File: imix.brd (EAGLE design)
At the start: 87 x 102.5 mm, 161 parts, among them Q1 AO3418, Q2 AO3415, Q3 AO3415, Q4 AO3415, Q5 AO3415, U1 BQ2423X, U10 ISL29035, U11 FX0S8700CQ, U12 296-12686-1-ND, U3 TLV3202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

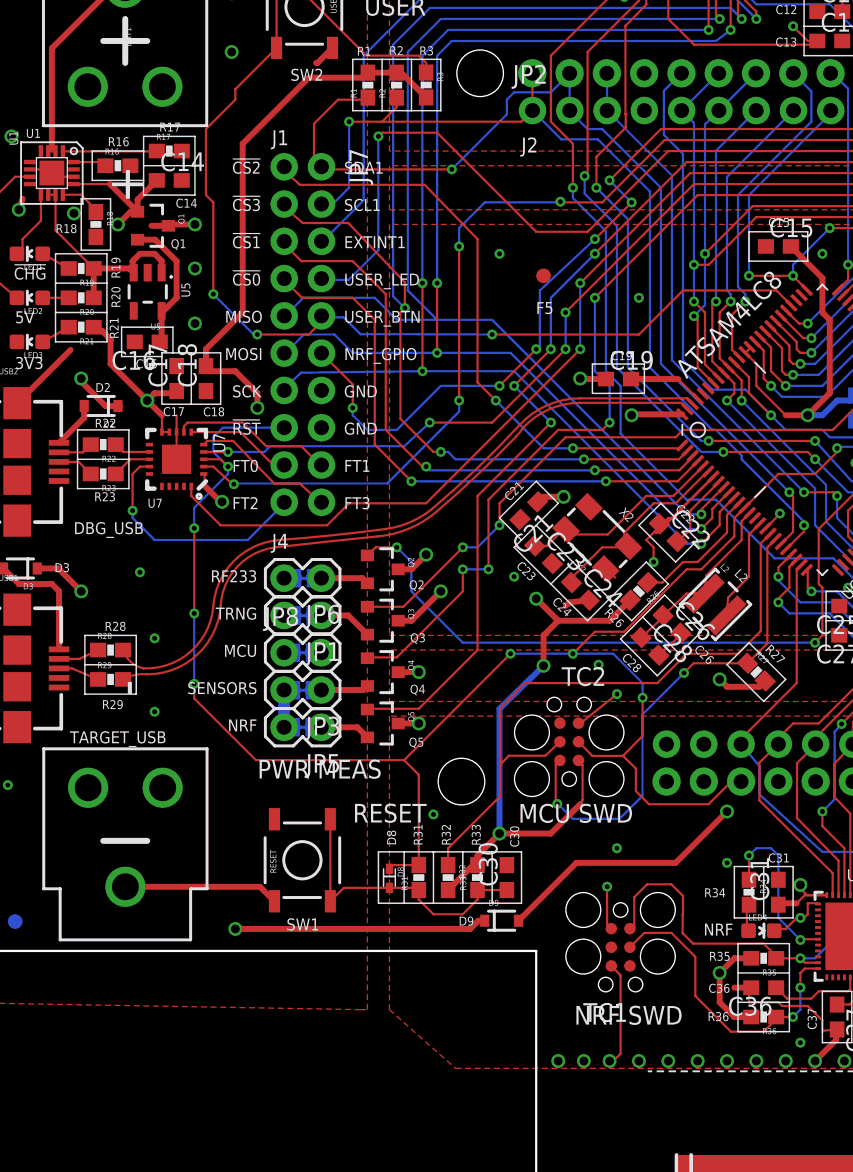
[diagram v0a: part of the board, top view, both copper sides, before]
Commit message: Move MCU SWD to be accessible when a shield is present
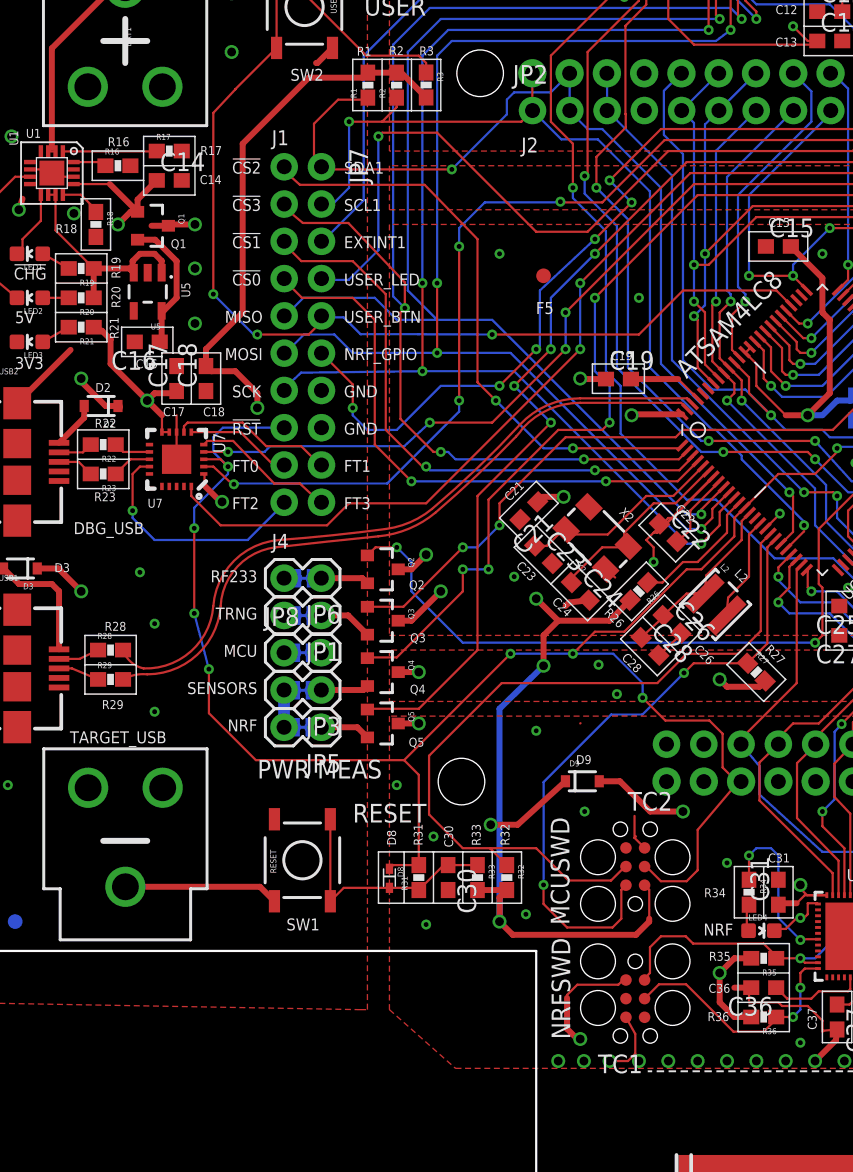
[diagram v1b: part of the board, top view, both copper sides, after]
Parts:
- moved D9 11.0 mm to (40.6, 11.6)
- moved TC2 9.62 mm to (44.2, 5.75)
- moved C30 4.00 mm to (31.5, 5.00), turned to 270 degrees
- moved R32 4.00 mm to (35.5, 5.00)
- moved TC1 3.64 mm to (44.2, -3.25)
- turned R33 to 270 degrees
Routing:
- net VCC_IN: track 96.0 -> 83.6 mm
- net SWDCLK/TCK: track 43.7 -> 54.3 mm
- net SWDIO/TMS: track 33.4 -> 43.4 mm
- net VCC_MCU_3V3: track 165.6 -> 174.6 mm
- net VCC_EXT_5V: track 78.4 -> 70.7 mm
- net NRF_SWDIO: track 77.5 -> 73.4 mm
- net NRF_SWDCLK: track 21.1 -> 17.1 mm
- net VCC_SENSE_3V3: track 91.4 -> 87.6 mm
- net N$8: track 20.2 -> 16.8 mm
- net GND: track 166.1 -> 162.7 mm, vias 80 -> 84
- net VCC_NRF_3V3: track 51.8 -> 54.9 mm
- net !RESET: track 140.6 -> 143.4 mm
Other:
- board text added: "MCUSWD"
- board text added: "NRFSWD"
- board text removed: "MCU SWD"
- board text removed: "NRF SWD"

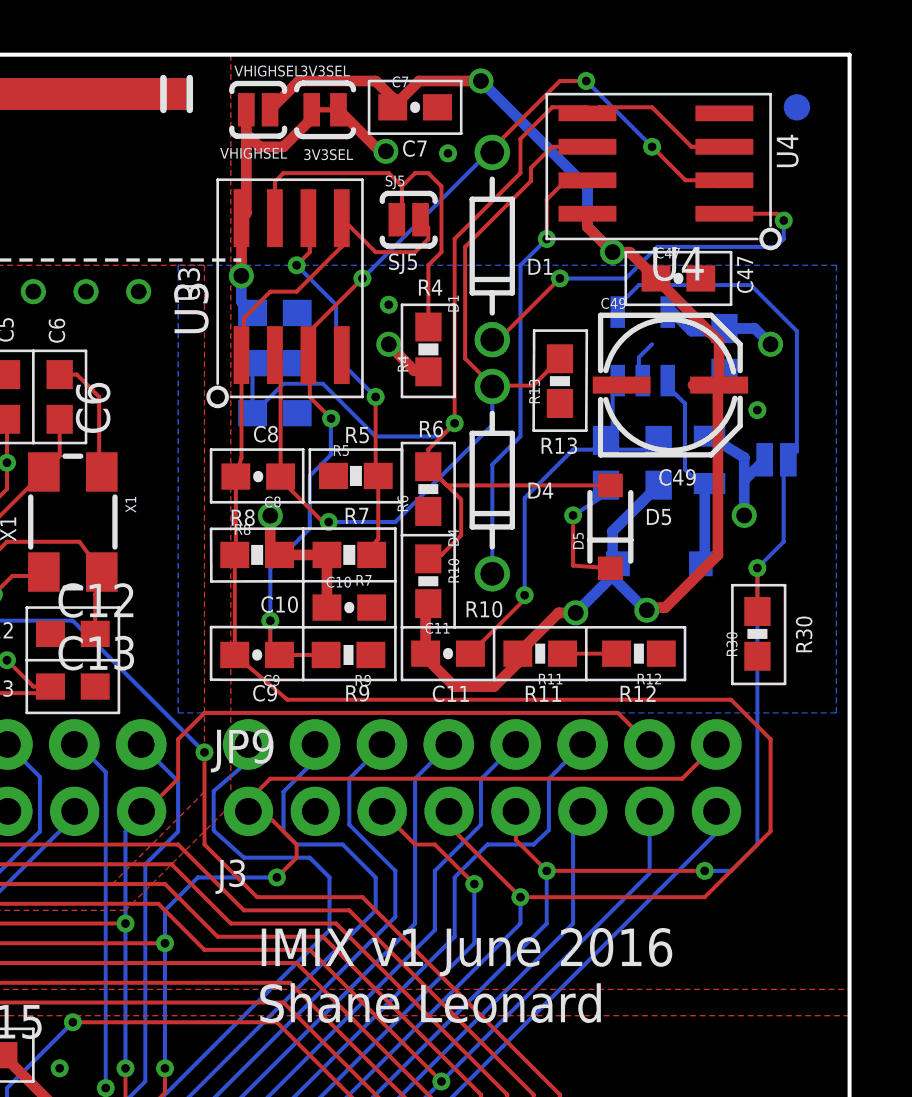
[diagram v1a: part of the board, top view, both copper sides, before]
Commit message: Refactor RNG
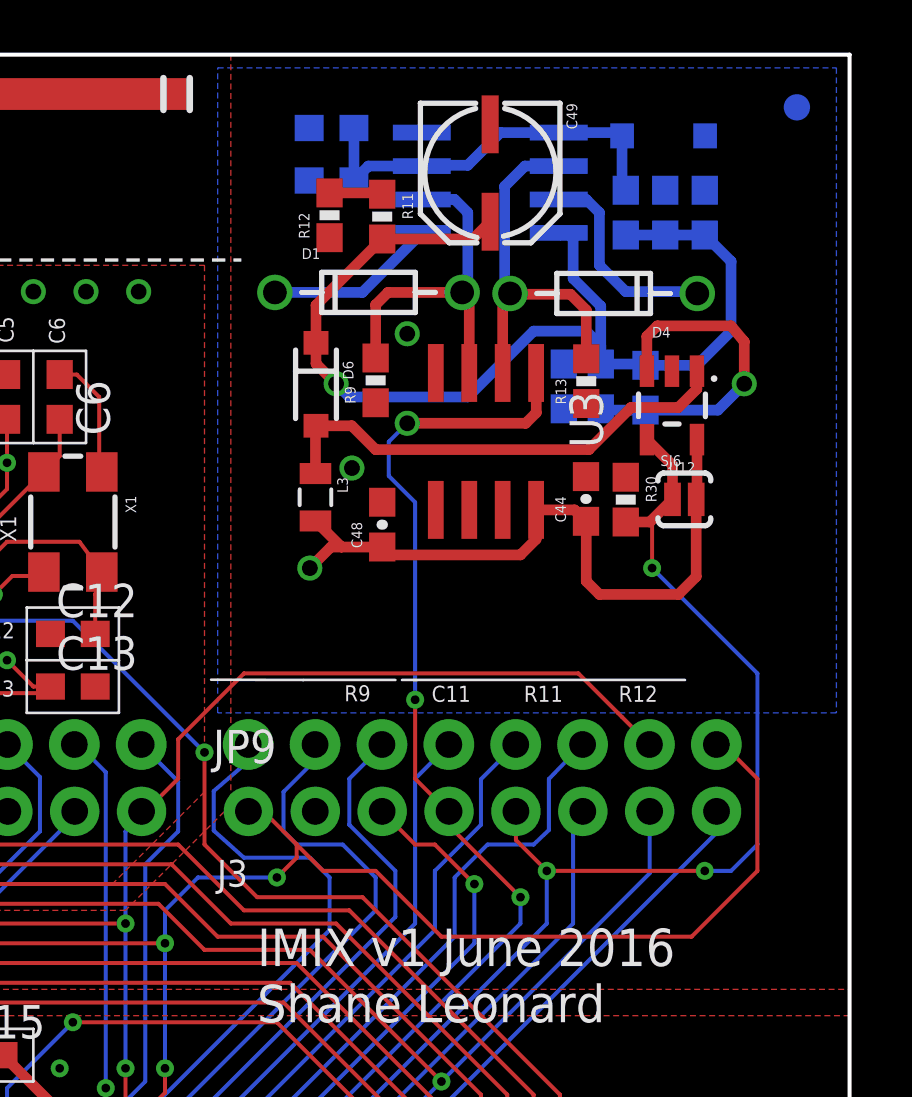
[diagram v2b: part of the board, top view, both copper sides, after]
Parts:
- removed 3V3SEL: SOLDERJUMPER-OLDTRACE, SparkFun-Retired:SJ_2S-TRACE
- removed C10, C8, C9: DNP, SparkFun-Capacitors:0603-CAP
- removed R4, R5, R7, R8: DNP, SparkFun-Passives:0603-RES
- removed R6: DNP, SparkFun-Resistors:0603-RES
- removed SJ5: SOLDERJUMPERNO, SparkFun-Retired:SJ_2S-NO
- removed VHIGHSEL: SOLDERJUMPER-OLDNO, SparkFun-Retired:SJ_2S-NO
- moved R12 20.4 mm to (67.2, 79.9), turned to 90 degrees
- moved R11 17.7 mm to (69.2, 79.8), turned to 270 degrees
- moved R10 15.9 mm to (78.5, 80.0), flipped to the bottom
- moved L3 15.0 mm to (66.7, 69.2), flipped to the top, turned to 270 degrees
- moved D5 15.0 mm to (79.9, 82.9), flipped to the bottom, turned to 0 degrees
- moved D6 14.7 mm to (66.7, 73.5), flipped to the top, turned to 270 degrees
- moved C48 14.6 mm to (69.2, 68.2), flipped to the top, turned to 90 degrees
- moved C44 13.8 mm to (77.0, 69.1), flipped to the top, turned to 90 degrees
- moved C11 12.6 mm to (79.2, 73.3), flipped to the bottom, turned to 270 degrees
- moved R9 10.5 mm to (69.0, 73.6), turned to 90 degrees
- moved C7 10.3 mm to (80.0, 80.0), flipped to the bottom, turned to 90 degrees
- moved C49 10.3 mm to (73.5, 81.6), turned to 270 degrees
- moved U3 9.44 mm to (73.2, 71.3), turned to 180 degrees
- moved C45 9.19 mm to (67.3, 83.2), turned to 0 degrees
- moved C46 9.10 mm to (67.3, 81.2), turned to 0 degrees
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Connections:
- removed net BUFFER: R4.2, SJ5.1, U3.7
- removed net N$67: R5.2, R7.1, U3.6
- removed net N$68: 3V3SEL.1, C44.1, U3.8, VHIGHSEL.1
- net GND: no longer C10.2, R5.1, R6.1
- net N$66: no longer R6.2
- net NOISE1: no longer C9.1
- net NOISE2: no longer C8.1
- net TRNG_OUT: no longer C8.2, C9.2, R8.1, SJ5.2, U3.5
- net VCC_TRNG_3V3: now also C44.1, U3.8; no longer 3V3SEL.2, C10.1, R4.1, R7.2, R8.2
- net VHIGH: no longer VHIGHSEL.2
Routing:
- net TRNG_OUT: track 83.1 -> 45.4 mm, vias 2 -> 4
- net N$66: track 46.3 -> 15.1 mm, vias 1 -> 0
- net NOISE1: track 37.1 -> 13.7 mm, vias 5 -> 0
- net NOISE2: track 32.3 -> 14.7 mm, vias 1 -> 0
- net BUFFER: track 15.4 -> 0.00 mm
- net VHIGH: track 57.3 -> 42.0 mm, vias 4 -> 1
- net N$67: track 14.4 -> 0.00 mm, vias 2 -> 0
- net TRNG_EN: track 62.5 -> 50.2 mm
- net N$68: track 11.4 -> 0.00 mm, vias 1 -> 0
- net N$43: track 8.52 -> 18.3 mm
- net N$51: track 15.7 -> 6.52 mm, vias 2 -> 0
- net N$52: track 17.0 -> 7.91 mm, vias 1 -> 0
- net GND: track 162.7 -> 155.2 mm, vias 84 -> 82
- net VCC_TRNG_3V3: track 96.6 -> 103.5 mm, vias 6 -> 2
- net USART3_RX: track 93.0 -> 99.5 mm
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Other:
- board text removed: "3V3SEL"
- board text removed: "C10"
- board text removed: "C8"
- board text removed: "C9"
- board text removed: "F2"
- board text removed: "R4"
- board text removed: "R5"
- board text removed: "R6"
- board text removed: "R7"
- board text removed: "R8"
- board text removed: "SJ5"
- board text removed: "SJ6"
- board text removed: "VHIGHSEL"

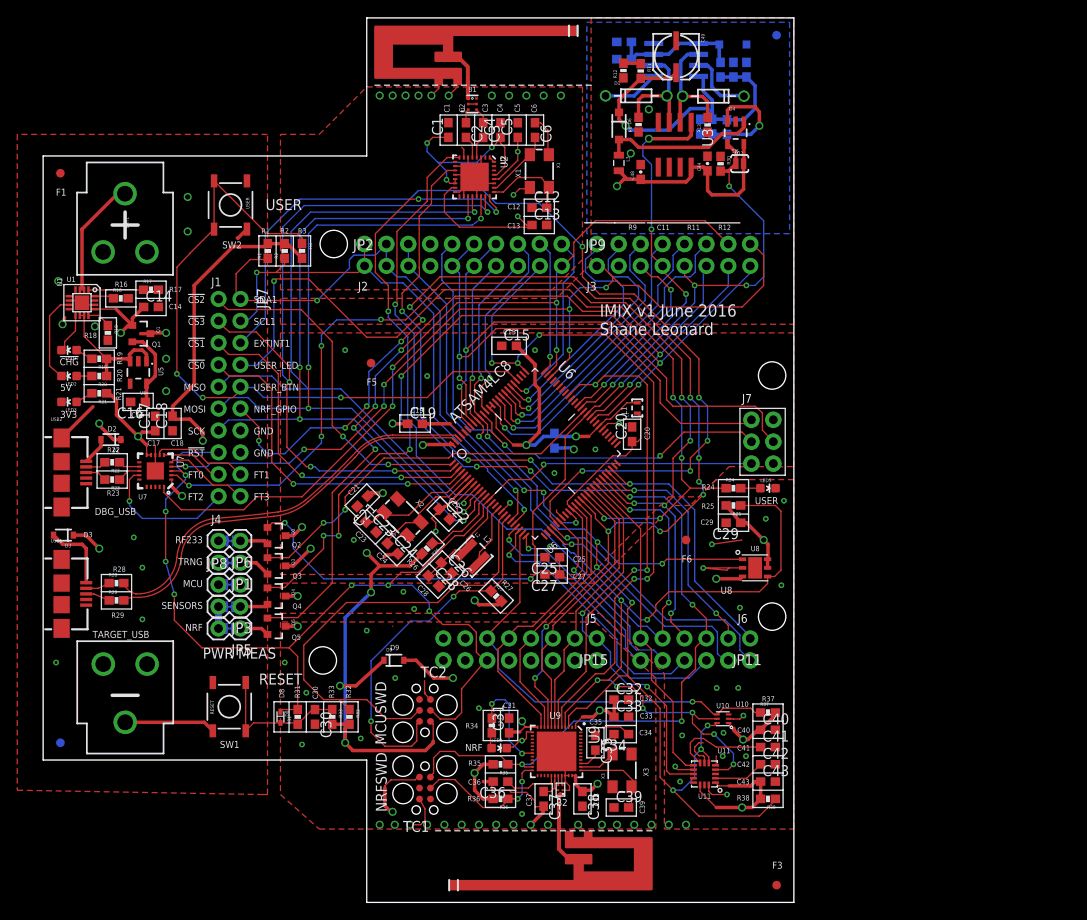
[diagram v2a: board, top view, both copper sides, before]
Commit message: Updated version incorporating several suggestions, still rerouting RNG
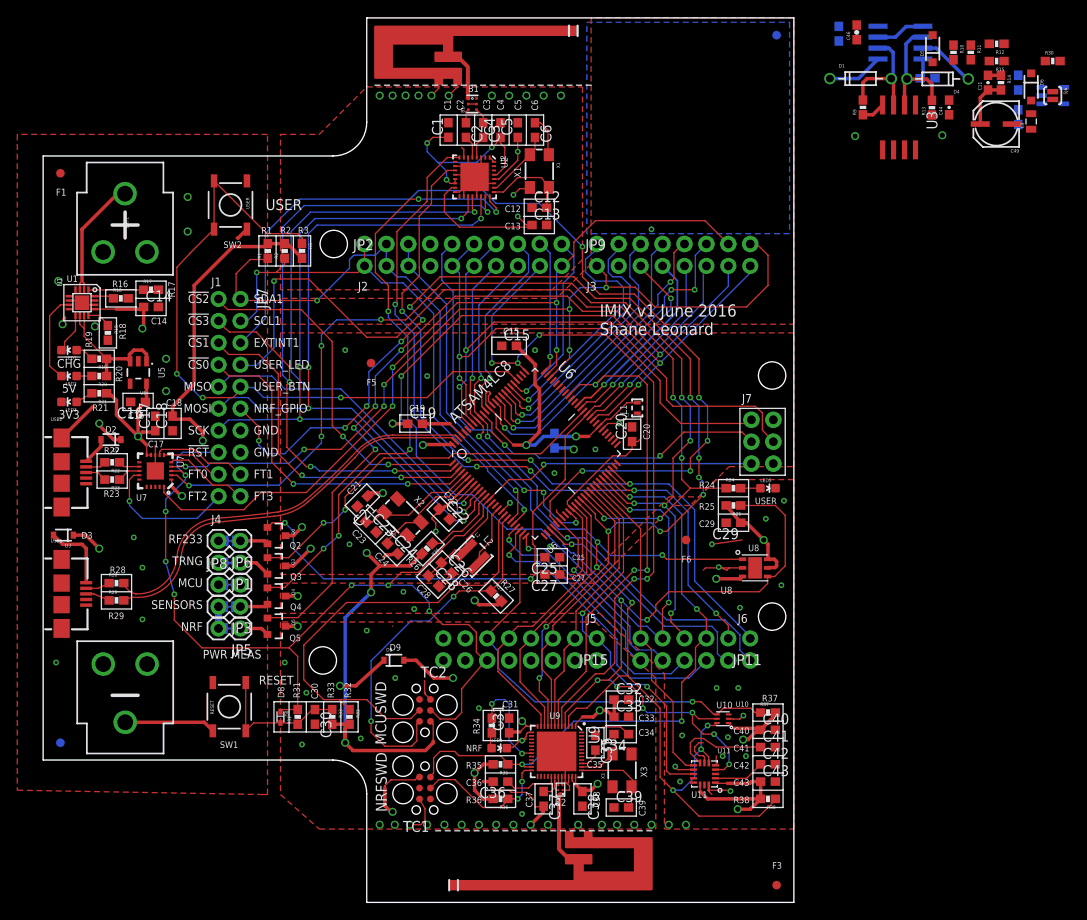
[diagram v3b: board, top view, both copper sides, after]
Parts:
- removed Q1: AO3418, SparkFun-DiscreteSemi:SOT23-3
- moved L3 48.0 mm to (114.5, 74.0), turned to 90 degrees
- moved D6 48.0 mm to (114.5, 78.0)
- moved C48 44.2 mm to (113.0, 74.5), flipped to the bottom
- moved R12 43.4 mm to (110.5, 83.0), turned to 180 degrees
- moved R30 40.3 mm to (117.0, 81.0), turned to 0 degrees
- moved R11 38.3 mm to (107.5, 82.0)
- moved C49 37.8 mm to (110.5, 73.5), turned to 180 degrees
- moved SJ6 37.1 mm to (117.0, 77.0), turned to 270 degrees
- moved U12 37.0 mm to (117.0, 77.0), flipped to the bottom, turned to 90 degrees
- moved R15 35.2 mm to (110.5, 81.0), flipped to the top, turned to 180 degrees
- moved R14 33.8 mm to (111.0, 78.5), flipped to the top, turned to 270 degrees
- moved C47 31.5 mm to (113.0, 78.5), turned to 270 degrees
- moved C11 30.7 mm to (109.5, 78.5), flipped to the top, turned to 90 degrees
- moved C44 28.7 mm to (105.0, 75.6)
- moved C46 27.1 mm to (94.3, 84.3), flipped to the top, turned to 90 degrees
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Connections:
- removed net VCC: C16.1, Q1.2, U5.5
- net VCC_3V3: now also C16.1, U5.5; no longer Q1.3
- net VCC_IN: no longer Q1.1
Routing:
- net VHIGH: track 42.0 -> 8.18 mm, vias 1 -> 0
- net TRNG_EN: track 50.2 -> 22.2 mm, vias 4 -> 1
- net VCC_TRNG_3V3: track 103.5 -> 77.5 mm, vias 2 -> 1
- net TRNG_OUT: track 45.4 -> 22.0 mm, vias 4 -> 2
- net N$43: track 18.3 -> 0.00 mm
- net N$46: track 14.4 -> 1.50 mm, vias 1 -> 0
- net N$66: track 15.1 -> 5.73 mm
- net VCC: track 9.29 -> 0.00 mm
- net VCC_SENSE_3V3: track 87.6 -> 92.6 mm
- net VCC_MCU_3V3: track 174.6 -> 178.4 mm
- net VCC_3V3: track 84.0 -> 87.5 mm, vias 3 -> 2
- net GND: track 155.2 -> 158.5 mm
- net VHIGHSAMPLE: track 2.02 -> 0.00 mm
- net GPIO6: track 31.2 -> 29.9 mm
- net VCC_LDO: track 15.5 -> 16.7 mm
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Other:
- outline, holes or cut-outs redrawn
- board text removed: "R11"
- board text removed: "R12"
